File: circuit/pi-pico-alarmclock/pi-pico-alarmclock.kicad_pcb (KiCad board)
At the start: 2 copper layers, 79.8 x 80.5 mm, 33 parts, among them J1 Screw_Terminal_2_P5.00mm, J2 BTN GREEN, J3 BTN BLUE, J4 BTN_YELLOW, J5 NEOPIXEL, J6 OLED, J7 BAT, Q1 IRLZ44N, Q3 IRF9540, Q4 IRLZ44N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

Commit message: pcb and schemativ v0.2: Fix ground bounce by providing direct path to battery ground
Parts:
- J7: value BAT -> BAT - Screw_Terminal_2_P5.00mm
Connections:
- J7 pad 2: /BAT- -> GND
- U3 pad 6: /BAT- -> GND
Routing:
- net GND: track 18.7 -> 35.4 mm
- net /BAT-: track 16.7 -> 0.00 mm
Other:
- board text added: "1-rafael-1 Pi Pico Alarmclock V0.2 / 11.2025"
- board text removed: "1-rafael-1 Pi Pico Alarmclock V0.1 / 11.2025"

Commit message: Correct GPIO nets, update placements and values
Rename GPIO nets (GP14/GP15/GP19) and Q2 nets; adjust pad pintypes.
Reposition multiple footprints and update silk/fab layers. Change
resistor values (1M -> 200K, 680k -> 100K). Add PCB .stl step file, plus
GND symbols and a 100nF decoupling cap.
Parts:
- added C5: 100nF_Ceramic, Capacitor_THT:C_Disc_D5.0mm_W2.5mm_P2.50mm, F.Cu at (180.8, 81.2)
- added C8: 100nF_Ceramic, Capacitor_THT:C_Disc_D5.0mm_W2.5mm_P2.50mm, F.Cu at (179.2, 69.5)
- added Q2: IRLZ44N, PCM_Package_TO_SOT_THT_AKL:TO-220-3_Vertical_GDS, F.Cu at (113.2, 100.2)
- added R13: 100ohm, Resistor_THT:R_Axial_DIN0207_L6.3mm_D2.5mm_P10.16mm_Horizontal, F.Cu at (126.7, 84.5)
- added R14: 10k, Resistor_THT:R_Axial_DIN0207_L6.3mm_D2.5mm_P10.16mm_Horizontal, F.Cu at (122.8, 111.1)
- R10, R12: value 1M -> 200K
- R11, R9: value 680k -> 100K
- moved R3 13.3 mm to (141.6, 49.2), turned to 180 degrees
- moved R1 5.10 mm to (121.8, 94.5)
- moved R2 4.61 mm to (111.6, 91.2)
- moved C4 4.18 mm to (114.5, 124.8)
- moved Q1 4.12 mm to (113.2, 86.7)
- moved C2 3.44 mm to (112.8, 109.5)
- moved C7 3.05 mm to (112.8, 118.5)
- moved C3 2.57 mm to (129.8, 107.0)
- moved D1 2.47 mm to (132.8, 72.2)
- moved C1 2.29 mm to (135.2, 57.2)
- moved J1 1.53 mm to (113.2, 52.0)
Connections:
- J5 pad 1: GND -> Net-(Q2-D)
- J5 pad 3: /GP19 -> /GP15
- U1 pad 19: unconnected-(U1-GPIO14-Pad19) -> /GP14
- U1 pad 20: unconnected-(U1-GPIO15-Pad20) -> /GP15
- U1 pad 25: /GP19 -> unconnected-(U1-GPIO19-Pad25)
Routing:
- net /GP19: track 41.0 -> 0.00 mm, vias 1 -> 0
- net Net-(Q2-G): track 0.00 -> 31.7 mm
- net +5V: track 95.5 -> 124.2 mm
- net /GP14: track 0.00 -> 17.5 mm, vias 0 -> 1
- net /GP15: track 0.00 -> 16.5 mm
- net Net-(Q2-D): track 0.00 -> 14.5 mm
- net GND: track 35.4 -> 27.1 mm
- net /GP27: track 13.4 -> 20.8 mm
- net /GP28: track 17.3 -> 23.3 mm
- net /GP3: track 32.2 -> 27.2 mm
- net Net-(D1-USART_RX): track 16.9 -> 14.4 mm
- net /GP6: track 48.0 -> 50.4 mm, vias 1 -> 2
- net Net-(Q1-D): track 28.7 -> 27.6 mm
- net Net-(D1-Speaker_-): track 13.7 -> 12.9 mm
- net Net-(D1-Speaker_+): track 13.7 -> 12.8 mm
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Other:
- board text added: "1-rafael-1 Pi Pico Alarmclock V0.3 / 12.2025"
- board text added: "GP"
- board text added: "LG"
- board text added: "LV"
- board text removed: "1-rafael-1 Pi Pico Alarmclock V0.2 / 11.2025"

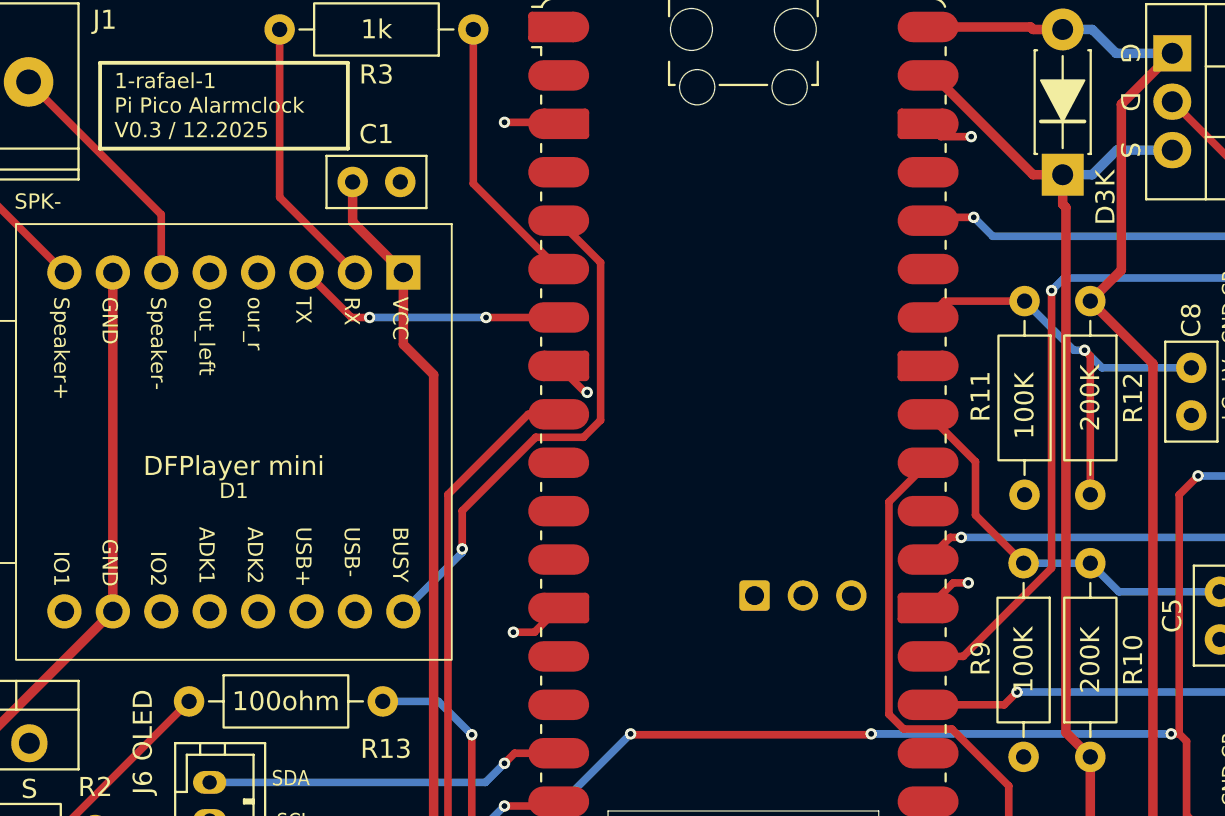
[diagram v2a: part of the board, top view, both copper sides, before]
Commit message: Update resistors to 220K and bump revision
Set several 200K resistor values to 220K in schematic and PCB. Bump
project version/revision to v0.4 (01.2026 / 2026-01-06). Regenerate PCB
footprint UUIDs.
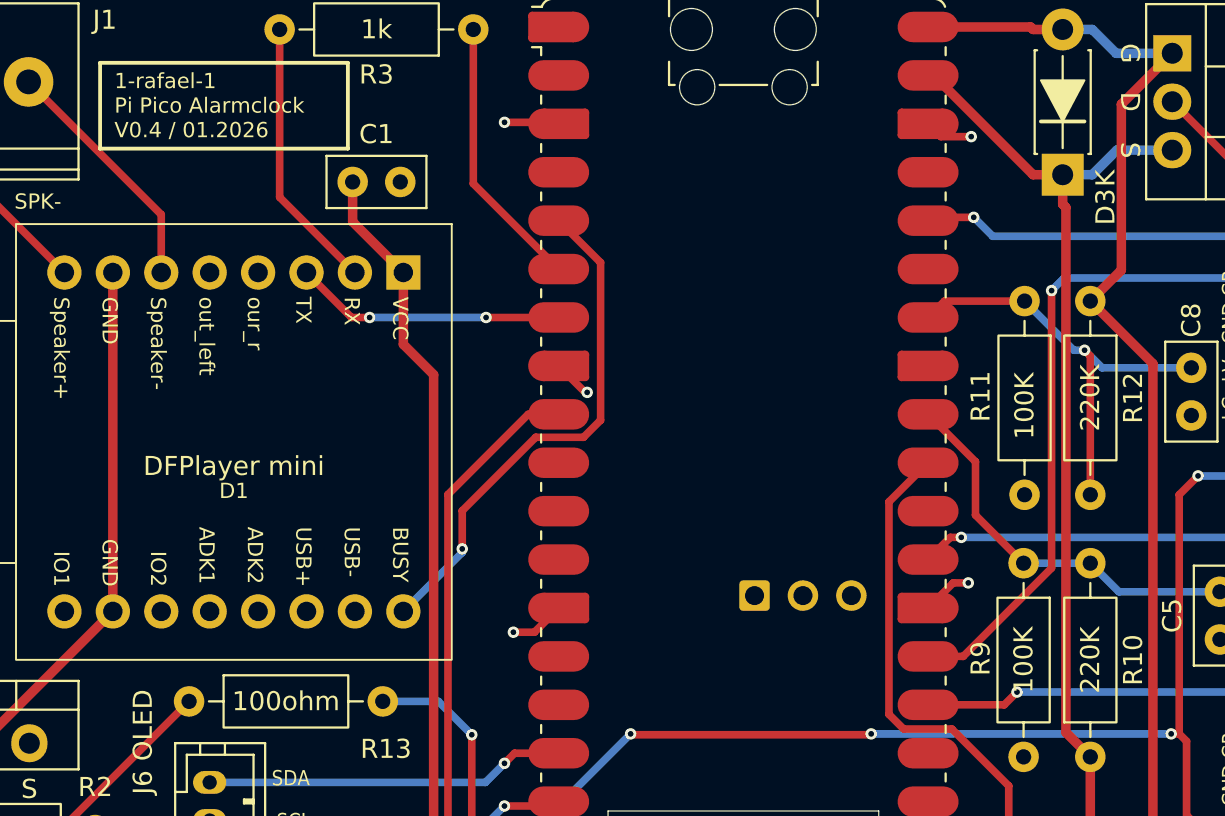
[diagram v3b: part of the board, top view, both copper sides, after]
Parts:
- R10, R12: value 200K -> 220K
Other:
- board text added: "1-rafael-1 Pi Pico Alarmclock V0.4 / 01.2026"
- board text removed: "1-rafael-1 Pi Pico Alarmclock V0.3 / 12.2025"
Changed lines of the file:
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@@
 			)
 		)
-		(property "Value" "200K"
+		(property "Value" "220K"
 			(at 5.08 0 90)
 			(layer "F.SilkS")
@@
 			)
 		)
-		(property "Value" "200K"
+		(property "Value" "220K"
 			(at 5.08 0 90)
 			(layer "F.SilkS")
@@
 		)
 	)
-	(gr_text "1-rafael-1\nPi Pico Alarmclock\nV0.3 / 12.2025"
+	(gr_text "1-rafael-1\nPi Pico Alarmclock\nV0.4 / 01.2026"
 		(at 122.75 55 0)
 		(layer "F.SilkS")
